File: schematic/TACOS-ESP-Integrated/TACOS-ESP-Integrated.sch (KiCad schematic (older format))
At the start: 12 parts, among them J2 MRC522, J3 Relay, SW1 SW_ARM, U1 WeMos_D1_mini

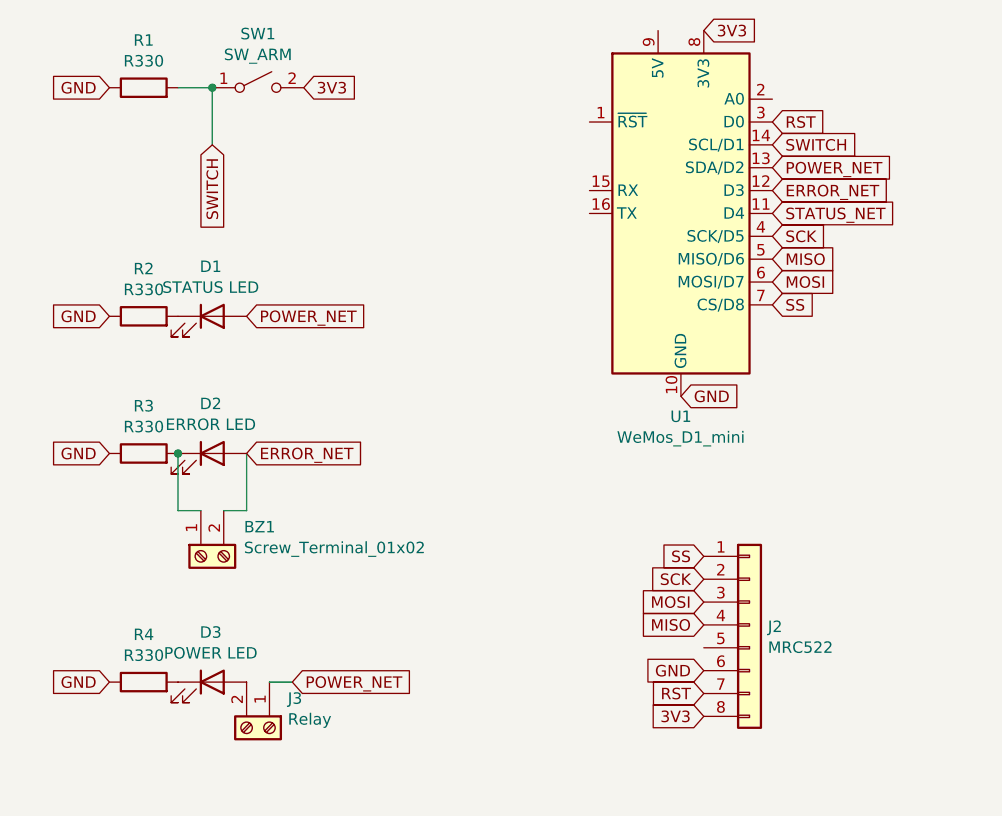
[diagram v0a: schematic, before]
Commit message: Schematic updates
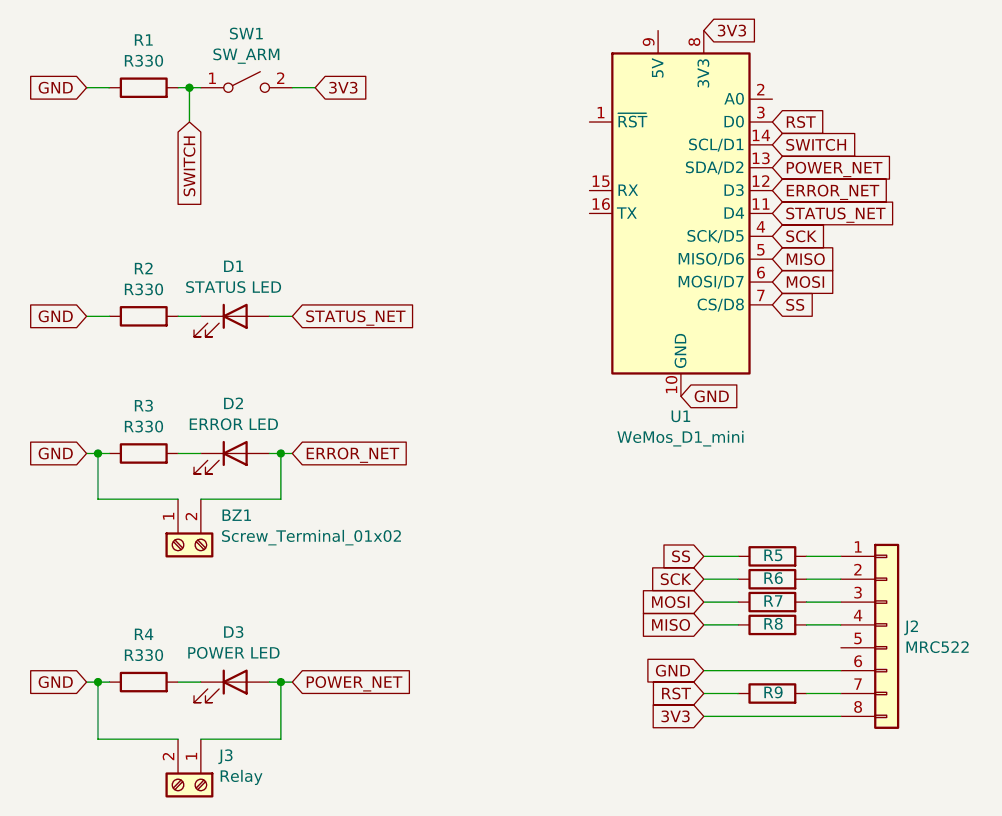
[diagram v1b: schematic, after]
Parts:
- added R5, R6, R7, R8, R9: R100, Resistor_SMD:R_0603_1608Metric, symbol Device:R
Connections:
- net GND: now also BZ1.1 (Pin_1), J3.2 (Pin_2)
- net MISO: now also R8.1; no longer J2.4 (Pin_4)
- net MOSI: now also R7.1; no longer J2.3 (Pin_3)
- net POWER_NET: now also D3.2 (A); no longer D1.2 (A)
- net RST: now also R9.1; no longer J2.7 (Pin_7)
- net SCK: now also R6.1; no longer J2.2 (Pin_2)
- net SS: now also R5.1; no longer J2.1 (Pin_1)
- net STATUS_NET: now also D1.2 (A)
- net at D2.1 (K), R3.2: no longer BZ1.1 (Pin_1)
- new net: J2.1 (Pin_1), R5.2
- new net: J2.2 (Pin_2), R6.2
- new net: J2.3 (Pin_3), R7.2
- new net: J2.4 (Pin_4), R8.2
- new net: J2.7 (Pin_7), R9.2
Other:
- moved on the sheet: BZ1, D1, D2, D3, J2, J3, SW1
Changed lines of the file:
@@
 L Device:LED D1
 U 1 1 5F287C44
-P 1900 3050
-F 0 "D1" H 1893 3267 50  0000 C CNN
-F 1 "STATUS LED" H 1893 3176 50  0000 C CNN
-F 2 "TerminalBlock:TerminalBlock_bornier-2_P5.08mm" H 1900 3050 50  0001 C CNN
-F 3 "~" H 1900 3050 50  0001 C CNN
-	1    1900 3050
+P 2000 3050
+F 0 "D1" H 1993 3267 50  0000 C CNN
+F 1 "STATUS LED" H 1993 3176 50  0000 C CNN
+F 2 "TerminalBlock:TerminalBlock_bornier-2_P5.08mm" H 2000 3050 50  0001 C CNN
+F 3 "~" H 2000 3050 50  0001 C CNN
+	1    2000 3050
 	1    0    0    -1
 $EndComp
@@
 L Device:LED D2
 U 1 1 5F288087
-P 1900 3650
-F 0 "D2" H 1893 3867 50  0000 C CNN
-F 1 "ERROR LED" H 1893 3776 50  0000 C CNN
-F 2 "TerminalBlock:TerminalBlock_bornier-2_P5.08mm" H 1900 3650 50  0001 C CNN
-F 3 "~" H 1900 3650 50  0001 C CNN
-	1    1900 3650
+P 2000 3650
+F 0 "D2" H 1993 3867 50  0000 C CNN
+F 1 "ERROR LED" H 1993 3776 50  0000 C CNN
+F 2 "TerminalBlock:TerminalBlock_bornier-2_P5.08mm" H 2000 3650 50  0001 C CNN
+F 3 "~" H 2000 3650 50  0001 C CNN
+	1    2000 3650
 	1    0    0    -1
 $EndComp
@@
 L Device:LED D3
 U 1 1 5F2889AC
-P 1900 4650
-F 0 "D3" H 1893 4867 50  0000 C CNN
-F 1 "POWER LED" H 1893 4776 50  0000 C CNN
-F 2 "TerminalBlock:TerminalBlock_bornier-2_P5.08mm" H 1900 4650 50  0001 C CNN
-F 3 "~" H 1900 4650 50  0001 C CNN
-	1    1900 4650
+P 2000 4650
+F 0 "D3" H 1993 4867 50  0000 C CNN
+F 1 "POWER LED" H 1993 4776 50  0000 C CNN
+F 2 "TerminalBlock:TerminalBlock_bornier-2_P5.08mm" H 2000 4650 50  0001 C CNN
+F 3 "~" H 2000 4650 50  0001 C CNN
+	1    2000 4650
 	1    0    0    -1
 $EndComp
@@
 L Switch:SW_SPST SW1
 U 1 1 5F2894AE
-P 2100 2050
-F 0 "SW1" H 2100 2285 50  0000 C CNN
-F 1 "SW_ARM" H 2100 2194 50  0000 C CNN
-F 2 "TerminalBlock:TerminalBlock_bornier-2_P5.08mm" H 2100 2050 50  0001 C CNN
-F 3 "~" H 2100 2050 50  0001 C CNN
-	1    2100 2050
+P 2050 2050
+F 0 "SW1" H 2050 2285 50  0000 C CNN
+F 1 "SW_ARM" H 2050 2194 50  0000 C CNN
+F 2 "TerminalBlock:TerminalBlock_bornier-2_P5.08mm" H 2050 2050 50  0001 C CNN
+F 3 "~" H 2050 2050 50  0001 C CNN
+	1    2050 2050
 	1    0    0    -1
 $EndComp
@@
 	0    -1   -1   0
 $EndComp
-Text GLabel 1450 3050 0    50   Input ~ 0
-GND
-Text GLabel 1450 3650 0    50   Input ~ 0
-GND
-Text GLabel 2050 3050 2    50   Input ~ 0
-POWER_NET
-Text GLabel 2050 3650 2    50   Input ~ 0
+Text GLabel 1350 3050 0    50   Input ~ 0
+GND
+Text GLabel 1350 3650 0    50   Input ~ 0
+GND
+Text GLabel 2250 3650 2    50   Input ~ 0
 ERROR_NET
 Text GLabel 2250 4650 2    50   Input ~ 0
 POWER_NET
-Text GLabel 1450 4650 0    50   Input ~ 0
-GND
-Wire Wire Line
-	1750 3900 1750 3650
-Connection ~ 1750 3650
-Wire Wire Line
-	2050 3900 2050 3650
-Wire Wire Line
-	2150 4650 2250 4650
-Text GLabel 2300 2050 2    50   Input ~ 0
+Text GLabel 1350 4650 0    50   Input ~ 0
+GND
+Wire Wire Line
+	2150 4650 2200 4650
+Text GLabel 2350 2050 2    50   Input ~ 0
 3V3
 $Comp
@@
 	0    -1   -1   0
 $EndComp
-Wire Wire Line
-	1750 2050 1900 2050
-Text GLabel 1450 2050 0    50   Input ~ 0
-GND
-Text GLabel 1900 2300 3    50   Input ~ 0
+Text GLabel 1350 2050 0    50   Input ~ 0
+GND
+Text GLabel 1800 2200 3    50   Input ~ 0
 SWITCH
-Wire Wire Line
-	1900 2300 1900 2050
-Connection ~ 1900 2050
 $Comp
 L Connector_Generic:Conn_01x08 J2
 U 1 1 5F285F64
-P 4250 4400
-F 0 "J2" H 4330 4392 50  0000 L CNN
-F 1 "MRC522" H 4330 4301 50  0000 L CNN
-F 2 "Connector_PinHeader_2.54mm:PinHeader_1x08_P2.54mm_Vertical" H 4250 4400 50  0001 C CNN
-F 3 "~" H 4250 4400 50  0001 C CNN
-	1    4250 4400
+P 4850 4400
+F 0 "J2" H 4930 4392 50  0000 L CNN
+F 1 "MRC522" H 4930 4301 50  0000 L CNN
+F 2 "Connector_PinHeader_2.54mm:PinHeader_1x08_P2.54mm_Vertical" H 4850 4400 50  0001 C CNN
+F 3 "~" H 4850 4400 50  0001 C CNN
+	1    4850 4400
 	1    0    0    -1
 $EndComp
@@
 L Connector:Screw_Terminal_01x02 J3
 U 1 1 5F2B9C76
-P 2150 4850
-F 0 "J3" V 2022 4930 50  0000 L CNN
-F 1 "Relay" V 2113 4930 50  0000 L CNN
-F 2 "TerminalBlock:TerminalBlock_bornier-2_P5.08mm" H 2150 4850 50  0001 C CNN
-F 3 "~" H 2150 4850 50  0001 C CNN
-	1    2150 4850
+P 1850 5100
+F 0 "J3" V 1722 5180 50  0000 L CNN
+F 1 "Relay" V 1813 5180 50  0000 L CNN
+F 2 "TerminalBlock:TerminalBlock_bornier-2_P5.08mm" H 1850 5100 50  0001 C CNN
+F 3 "~" H 1850 5100 50  0001 C CNN
+	1    1850 5100
 	0    1    1    0
 $EndComp
-$Comp
-L Connector:Screw_Terminal_01x02 BZ1
-U 1 1 5F2C3AA2
-P 1850 4100
-F 0 "BZ1" V 1722 3912 50  0000 R CNN
-F 1 "Screw_Terminal_01x02" V 1813 3912 50  0000 R CNN
-F 2 "TerminalBlock:TerminalBlock_bornier-2_P5.08mm" H 1850 4100 50  0001 C CNN
-F 3 "~" H 1850 4100 50  0001 C CNN
-	1    1850 4100
-	0    -1   1    0
-$EndComp
-Wire Wire Line
-	1950 3900 2050 3900
-Wire Wire Line
-	1750 3900 1850 3900
 $Comp
 L MCU_Module:WeMos_D1_mini U1
@@
 Text GLabel 4350 2600 2    50   Input ~ 0
 STATUS_NET
+Text GLabel 2250 3050 2    50   Input ~ 0
+STATUS_NET
+Wire Wire Line
+	1450 3650 1400 3650
+Wire Wire Line
+	2150 3650 2200 3650
+Wire Wire Line
+	1850 3650 1750 3650
+$Comp
+L Connector:Screw_Terminal_01x02 BZ1
+U 1 1 5F2C3AA2
+P 1750 4050
+F 0 "BZ1" V 1622 3862 50  0000 R CNN
+F 1 "Screw_Terminal_01x02" V 1713 3862 50  0000 R CNN
+F 2 "TerminalBlock:TerminalBlock_bornier-2_P5.08mm" H 1750 4050 50  0001 C CNN
+F 3 "~" H 1750 4050 50  0001 C CNN
+	1    1750 4050
+	0    -1   1    0
+$EndComp
+Wire Wire Line
+	1850 3850 2200 3850
+Wire Wire Line
+	2200 3850 2200 3650
+Connection ~ 2200 3650
+Wire Wire Line
+	2200 3650 2250 3650
+Wire Wire Line
+	1750 3850 1400 3850
+Wire Wire Line
+	1400 3850 1400 3650
+Connection ~ 1400 3650
+Wire Wire Line
+	1400 3650 1350 3650
+Wire Wire Line
+	1350 3050 1450 3050
+Wire Wire Line
+	1750 3050 1850 3050
+Wire Wire Line
+	2150 3050 2250 3050
+Wire Wire Line
+	1450 2050 1350 2050
+Wire Wire Line
+	1850 2050 1800 2050
+Wire Wire Line
+	2350 2050 2250 2050
+Wire Wire Line
+	1800 2050 1800 2200
+Connection ~ 1800 2050
+Wire Wire Line
+	1800 2050 1750 2050
+Wire Wire Line
+	1350 4650 1400 4650
+Wire Wire Line
+	1850 4650 1750 4650
+Wire Wire Line
+	1750 4900 1400 4900
+Wire Wire Line
+	1400 4900 1400 4650
+Connection ~ 1400 4650
+Wire Wire Line
+	1400 4650 1450 4650
+Wire Wire Line
+	1850 4900 2200 4900
+Wire Wire Line
+	2200 4900 2200 4650
+Connection ~ 2200 4650
+Wire Wire Line
+	2200 4650 2250 4650
+$Comp
+L Device:R R5
+U 1 1 600954A4
+P 4350 4100
+F 0 "R5" V 4353 4096 50  0000 C CNN
+F 1 "R100" V 4466 4100 50  0001 C CNN
+F 2 "Resistor_SMD:R_0603_1608Metric" V 4280 4100 50  0001 C CNN
+F 3 "~" H 4350 4100 50  0001 C CNN
+	1    4350 4100
+	0    -1   -1   0
+$EndComp
+$Comp
+L Device:R R6
+U 1 1 6009B066
+P 4350 4200
+F 0 "R6" V 4353 4196 50  0000 C CNN
+F 1 "R100" V 4466 4200 50  0001 C CNN
+F 2 "Resistor_SMD:R_0603_1608Metric" V 4280 4200 50  0001 C CNN
+F 3 "~" H 4350 4200 50  0001 C CNN
+	1    4350 4200
+	0    -1   -1   0
+$EndComp
+$Comp
+L Device:R R7
+U 1 1 6009B537
+P 4350 4300
+F 0 "R7" V 4353 4296 50  0000 C CNN
+F 1 "R100" V 4466 4300 50  0001 C CNN
+F 2 "Resistor_SMD:R_0603_1608Metric" V 4280 4300 50  0001 C CNN
+F 3 "~" H 4350 4300 50  0001 C CNN
+	1    4350 4300
+	0    -1   -1   0
+$EndComp
+$Comp
+L Device:R R8
+U 1 1 6009B9F3
+P 4350 4400
+F 0 "R8" V 4353 4396 50  0000 C CNN
+F 1 "R100" V 4466 4400 50  0001 C CNN
+F 2 "Resistor_SMD:R_0603_1608Metric" V 4280 4400 50  0001 C CNN
+F 3 "~" H 4350 4400 50  0001 C CNN
+	1    4350 4400
+	0    -1   -1   0
+$EndComp
+$Comp
+L Device:R R9
+U 1 1 6009BE5B
+P 4350 4700
+F 0 "R9" V 4353 4696 50  0000 C CNN
+F 1 "R100" V 4466 4700 50  0001 C CNN
+F 2 "Resistor_SMD:R_0603_1608Metric" V 4280 4700 50  0001 C CNN
+F 3 "~" H 4350 4700 50  0001 C CNN
+	1    4350 4700
+	0    -1   -1   0
+$EndComp
+Wire Wire Line
+	4050 4100 4200 4100
+Wire Wire Line
+	4500 4100 4650 4100
+Wire Wire Line
+	4500 4200 4650 4200
+Wire Wire Line
+	4500 4300 4650 4300
+Wire Wire Line
+	4500 4400 4650 4400
+Wire Wire Line
+	4200 4400 4050 4400
+Wire Wire Line
+	4050 4300 4200 4300
+Wire Wire Line
+	4050 4200 4200 4200
+Wire Wire Line
+	4050 4700 4200 4700
+Wire Wire Line
+	4500 4700 4650 4700
+Wire Wire Line
+	4650 4600 4050 4600
+Wire Wire Line
+	4050 4800 4650 4800
 $EndSCHEMATC
